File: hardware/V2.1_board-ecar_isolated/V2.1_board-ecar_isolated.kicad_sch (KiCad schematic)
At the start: 108 parts, among them IC1 ATMEGA8A-P, J1 2x BATT IN, J10 24V, J11 18V, J12 5V, J13 ADC reserve, J14 IGBT [GND, Gate], J16 UART [TX, RX, GND], J17 2x Switch (to 5V), J18 Relay contacts [NO, COM, NC], J19 5V, 5V-decoupled, J2 ST 2x GND power, J21 ADC reserve, J22 ADC Gas-pedal, J23 2x 24V filtered, J24 Fan [GND-supp, Diode, Mosfet], J3 2x 24V filtered, J4 ST 2x GND 5V, J5 PWM-Signal, J6 LED 3,2V 20mA [-, +], J7 Gas Pedal, J8 Gate, J9 BATT, K1 24V relay, P1 ISP, Q1 BC547, Q2 IRFZ24N, U1 LM7818CT, U3 TC429, U4 LM358N

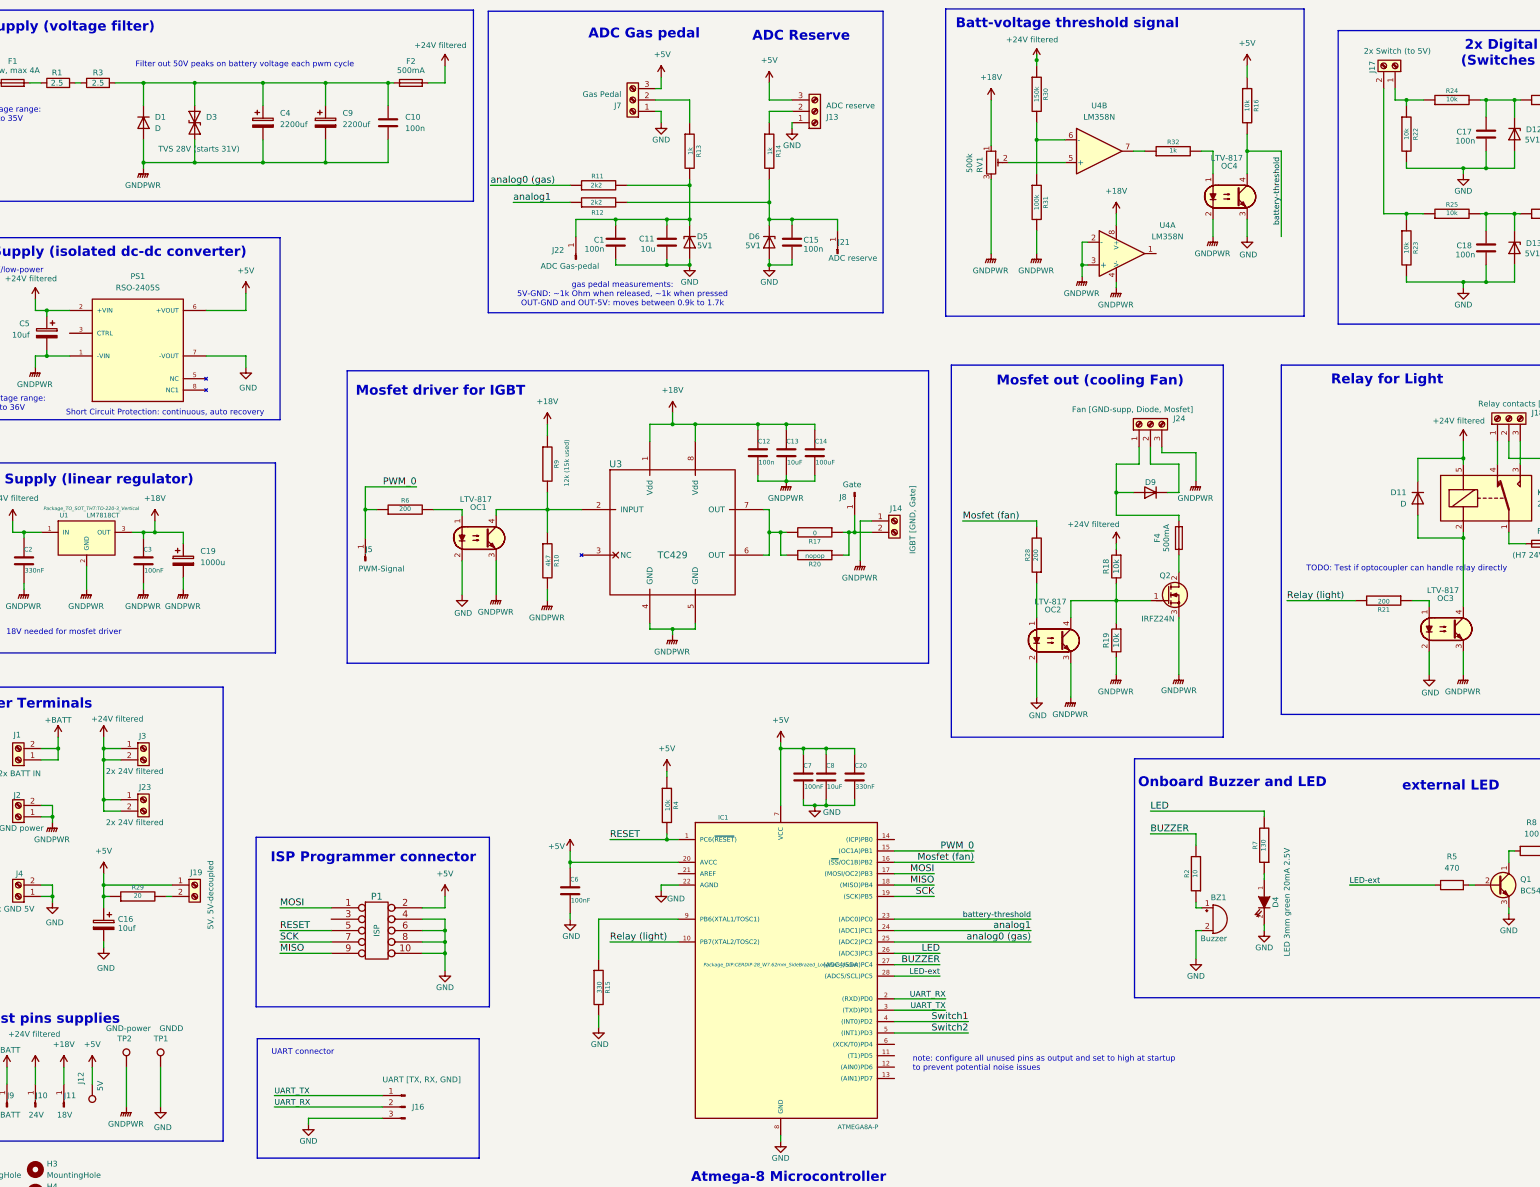
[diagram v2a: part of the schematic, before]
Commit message: pcb: optimize placement, assignment
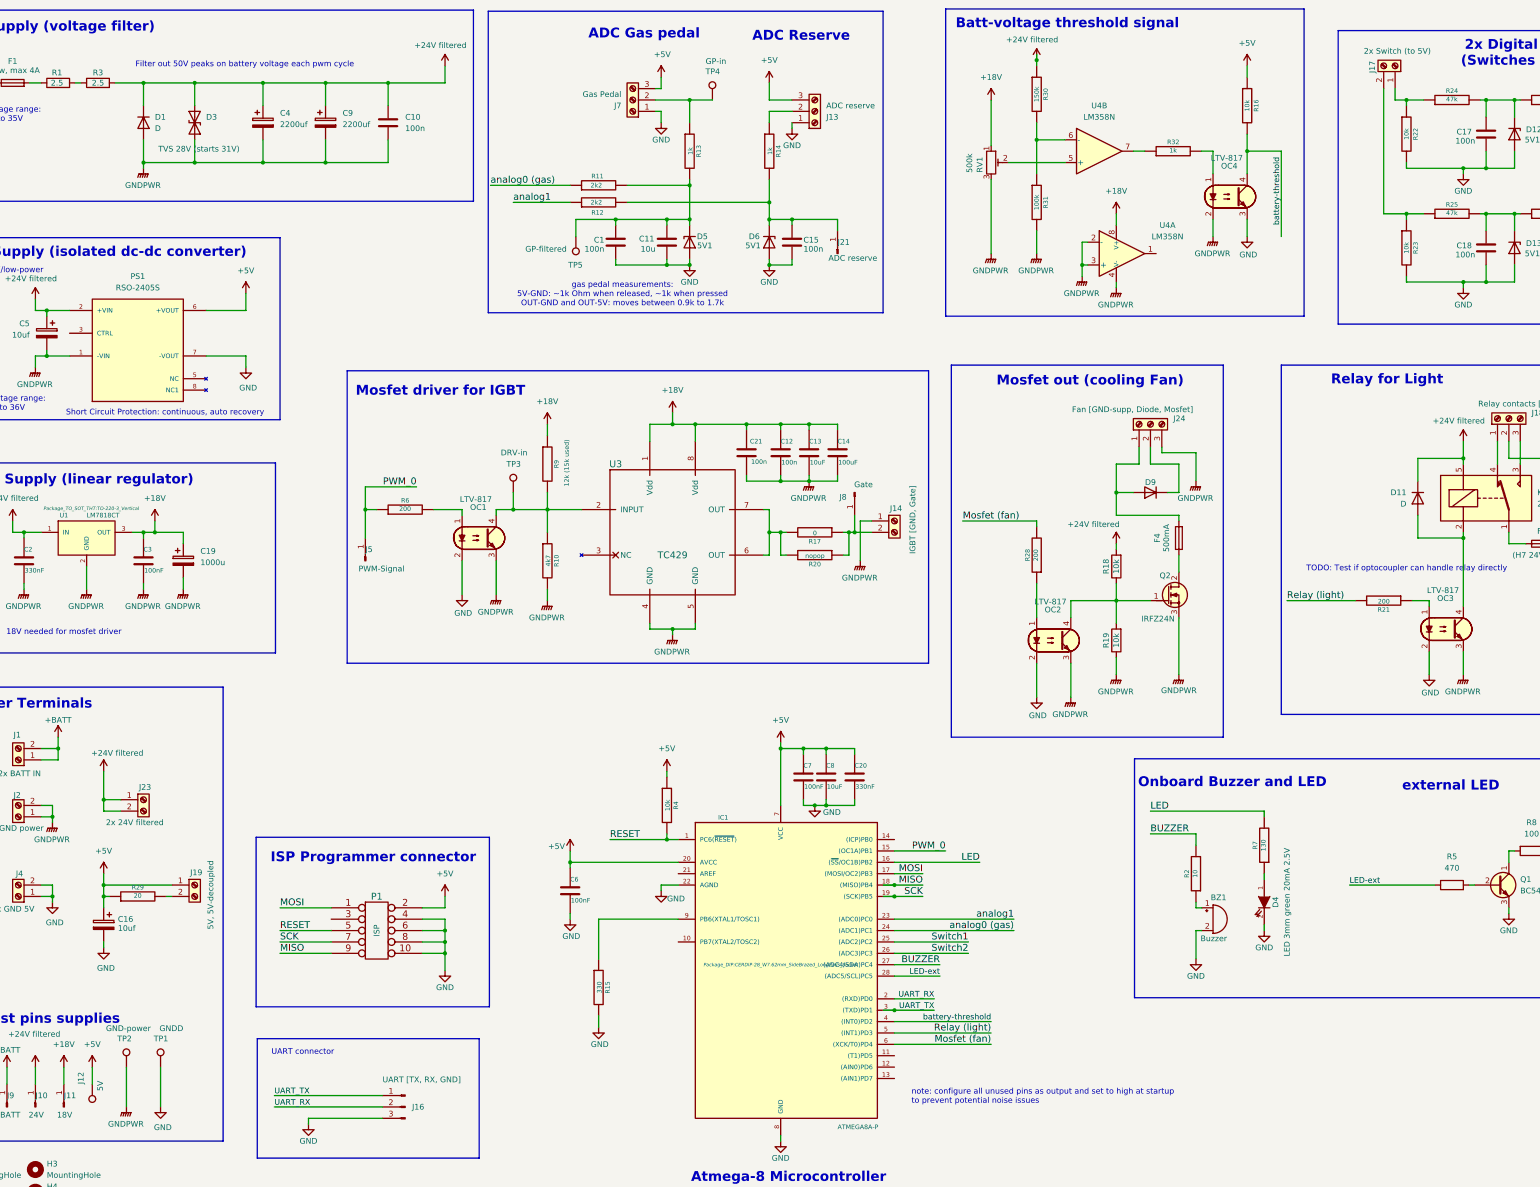
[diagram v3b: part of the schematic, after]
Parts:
- removed F2: 500mA, Fuse:Fuseholder_Cylinder-5x20mm_Stelvio-Kontek_PTF78_Horizontal_Open, symbol Device:Fuse
- removed J22: ADC Gas-pedal, Connector_PinHeader_1.00mm:PinHeader_1x01_P1.00mm_Vertical, symbol Connector:Conn_01x01_Pin
- removed J3: 2x 24V filtered, TerminalBlock:TerminalBlock_bornier-2_P5.08mm, symbol Connector:Screw_Terminal_01x02
- added C21: 100n, Capacitor_THT:C_Disc_D7.0mm_W2.5mm_P5.00mm, symbol treiber-rescue:C
- added TP3: DRV-in, Connector_PinHeader_1.00mm:PinHeader_1x01_P1.00mm_Vertical, symbol Connector:TestPoint
- added TP4: GP-in, Connector_PinHeader_1.00mm:PinHeader_1x01_P1.00mm_Vertical, symbol Connector:TestPoint
- added TP5: GP-filtered, Connector_PinHeader_1.00mm:PinHeader_1x01_P1.00mm_Vertical, symbol Connector:TestPoint
- R24, R25: value 10k -> 47k
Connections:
- net +18V: now also C21.1
- net +24V filtered: now also C10.1, C4.1, C9.1, D1.1 (K), D3.2 (A2), R3.2
- net GNDPWR: now also C21.2
- net LED: now also IC1.16 ((~{SS}/OC1B)PB2); no longer IC1.26 ((ADC3)PC3)
- net Mosfet (fan): now also IC1.6 ((XCK/T0)PD4); no longer IC1.16 ((~{SS}/OC1B)PB2)
- net Relay (light): now also IC1.5 ((INT1)PD3); no longer IC1.10 (PB7(XTAL2/TOSC2))
- net Switch1: now also IC1.25 ((ADC2)PC2); no longer IC1.4 ((INT0)PD2)
- net Switch2: now also IC1.26 ((ADC3)PC3); no longer IC1.5 ((INT1)PD3)
- net analog0 (gas): now also IC1.24 ((ADC1)PC1); no longer IC1.25 ((ADC2)PC2)
- net analog1: now also IC1.23 ((ADC0)PC0); no longer IC1.24 ((ADC1)PC1)
- net battery-threshold: now also IC1.4 ((INT0)PD2); no longer IC1.23 ((ADC0)PC0)
- net at C1.1, C11.1, D5.1 (K)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: now also TP5.1
- net at J7.2 (Pin_2), R13.1: now also TP4.1
- net at OC1.4, R10.1, R9.2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: now also TP3.1
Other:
- moved on the sheet: C12, C13, C14

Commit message: pcb: routing, pre gnd-plane
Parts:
- added R33: 2k2, Resistor_THT:R_Axial_DIN0207_L6.3mm_D2.5mm_P10.16mm_Horizontal, symbol control-rescue:R
- J13: value ADC reserve -> ADC reserve [5V, in, GND]
- J14: value IGBT [GND, Gate] -> IGBT [Gate, GND]
- J17: value 2x Switch (to 5V) -> 2x Switch (to 5V) [PC3, PC2]
- J19: value 5V, 5V-decoupled -> [5V, 5V-decoupled]
- J24: value Fan [GND-supp, Diode, Mosfet] -> Fan [GND/Mosfet-OUT, Diode, 24V-filtered]
- J4: value ST 2x GND 5V -> 2x GND (5V)
- J7: value Gas Pedal -> Gas Pedal [5V, In, GND]
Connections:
- net +24V filtered: now also J24.3 (Pin_3)
- net BUZZER: now also IC1.28 ((ADC5/SCL)PC5); no longer IC1.27 ((ADC4/SDA)PC4)
- net GNDPWR: now also J14.2 (Pin_2); no longer J14.1 (Pin_1), J24.3 (Pin_3)
- net LED: now also IC1.27 ((ADC4/SDA)PC4); no longer IC1.16 ((~{SS}/OC1B)PB2)
- net LED-ext: now also IC1.16 ((~{SS}/OC1B)PB2); no longer IC1.28 ((ADC5/SCL)PC5)
- net battery-threshold: now also R33.1; no longer OC4.4, R16.2
- net at J8.1 (Pin_1), R17.1, R20.1: now also J14.1 (Pin_1); no longer J14.2 (Pin_2)
- new net: OC4.4, R16.2, R33.2
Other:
- moved on the sheet: J14

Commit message: pcb: gnd-planes, testpoints, optimize, pcb2gcode - milling
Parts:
- added TP10: SW-filtered, Connector_PinHeader_1.00mm:PinHeader_1x01_P1.00mm_Vertical, symbol Connector:TestPoint
- added TP11: SW-in, Connector_PinHeader_1.00mm:PinHeader_1x01_P1.00mm_Vertical, symbol Connector:TestPoint
- added TP6: BATT, Connector_PinHeader_1.00mm:PinHeader_1x01_P1.00mm_Vertical, symbol Connector:TestPoint
- added TP7: OP -, Connector_PinHeader_1.00mm:PinHeader_1x01_P1.00mm_Vertical, symbol Connector:TestPoint
- added TP8: OP +, Connector_PinHeader_1.00mm:PinHeader_1x01_P1.00mm_Vertical, symbol Connector:TestPoint
- added TP9: OP out, Connector_PinHeader_1.00mm:PinHeader_1x01_P1.00mm_Vertical, symbol Connector:TestPoint
- J9: value BATT -> BATT-F
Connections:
- net at R30.2, R31.1, U4.6 (-): now also TP7.1
- net at OC4.1, R32.2: now also TP9.1
- net at J17.1 (Pin_1), R22.1, R24.1: now also TP11.1
- net at RV1.2, U4.5 (+): now also TP8.1
- net at F1.2, R1.1: now also TP6.1
- net at C17.1, D12.1 (K), R24.2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: now also TP10.1
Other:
- note added: "TODO: - Test if optocoupler can handle relay directly - Test minimal needed optocoupler led current (relay and digital input) - Test Isolated 5V supply IC (control pin unconnected)"
- note added: "TODO: Add hysteresis?"
- note removed: "TODO: Test if optocoupler can handle relay directly"
- moved on the sheet: J12, TP1, TP2

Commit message: pcb: optimize silk, change values
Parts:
- J16: value UART [TX, RX, GND] -> UART [GND, RX, TX]
- R21, R28: value 200 -> 510
- R32: value 1k -> 2k4
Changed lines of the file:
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@@
 			)
 		)
-		(property "Value" "UART [TX, RX, GND]"
+		(property "Value" "UART [GND, RX, TX]"
 			(at 113.03 254.254 0)
 			(effects
@@
 			)
 		)
-		(property "Value" "200"
+		(property "Value" "510"
 			(at 258.9022 137.1854 90)
 			(effects
@@
 			)
 		)
-		(property "Value" "200"
+		(property "Value" "510"
 			(at 336.5754 147.4978 90)
 			(effects
@@
 			)
 		)
-		(property "Value" "1k"
+		(property "Value" "2k4"
 			(at 289.5346 46.8122 90)
 			(effects

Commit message: V2.1 pcb finished, exports, photos, readme
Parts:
- R17: value 0 -> 10
- R9: value 12k (15k used) -> 15k
- TP3: value DRV-in -> Driver-in
- TP4: value GP-in -> Pedal-in
- TP5: value GP-filtered -> Pedal-filtered
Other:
- note added: "24V Relay: measured 16.7 mA at 30 V"
- note added: "CTRL Pin: high = OFF/low-power open = ON"
- note added: "External LED"
- note added: "Measurements with Optocoupler and 24V relay (15mA) 5 V, 200 Ohm -> I_led = 12 mA 5 V, 510 Ohm -> I_led = 7 mA, U_ce=0.7V 5 V, 820 Ohm -> I_led = 4.5 mA, U_ce=1.8V"
- note added: "Test-points supplies"
- note added: "note: its recommended to configure all unused pins as output and set to high at startup to prevent potential noise issues"
- note removed: "CTRL: high = OFF/low-power open = ON"
- note removed: "TODO: - Test if optocoupler can handle relay directly - Test minimal needed optocoupler led current (relay and digital input) - Test Isolated 5V supply IC (control pin unconnected)"
- note removed: "external LED"
- note removed: "note: configure all unused pins as output and set to high at startup to prevent potential noise issues"
- note removed: "test pins supplies"
- title: New version of PCB controlling an electric kart -> Second version of PCB controlling an electric kart
- moved on the sheet: BZ1, C1, C11, C12, C13, C14, C15, C17, C18, C19, C2, C21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
